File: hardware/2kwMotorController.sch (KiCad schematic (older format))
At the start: 0 parts

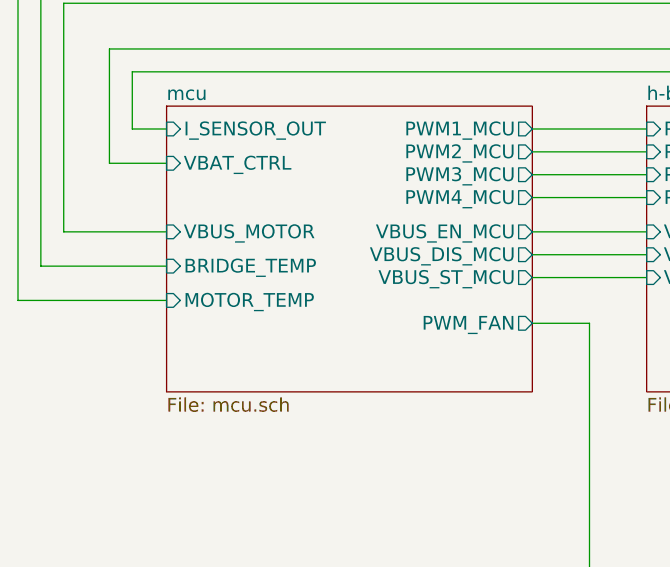
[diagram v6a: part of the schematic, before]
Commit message: Gate driver layout mostly complete
- Gate driver layout
- Switch LM5102 for UCC27211 (higher current, more robust)
- Tweak gate drive circuit passives
- No soldermask on high-current traces
- Fix error in orientation of LAH-100P footprint
- Improved draft layout of control section
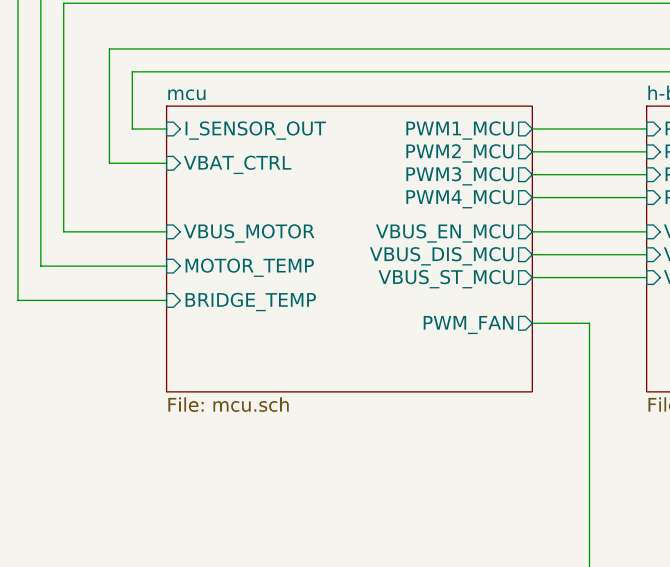
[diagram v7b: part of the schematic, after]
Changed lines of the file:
@@
 F9 "VBAT_CTRL" I L 3350 2200 60
 F10 "VBUS_MOTOR" I L 3350 2500 60
-F11 "BRIDGE_TEMP" I L 3350 2650 60
-F12 "MOTOR_TEMP" I L 3350 2800 60
-F13 "PWM_FAN" O R 4950 2900 60
-F14 "VBUS_ST_MCU" O R 4950 2700 60
+F11 "BRIDGE_TEMP" I L 3350 2800 60
+F12 "PWM_FAN" O R 4950 2900 60
+F13 "VBUS_ST_MCU" O R 4950 2700 60
+F14 "MOTOR_TEMP" I L 3350 2650 60
 $EndSheet
 Wire Wire Line
